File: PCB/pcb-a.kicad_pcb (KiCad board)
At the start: 2 copper layers, 109.7 x 43.5 mm, 44 parts, among them Q1 BC327, Q3 BC337, SW1 config, U1 MCP23008-xP, U2 MAX232I, U4 ATmega16L-8P, Y1 8Mhz

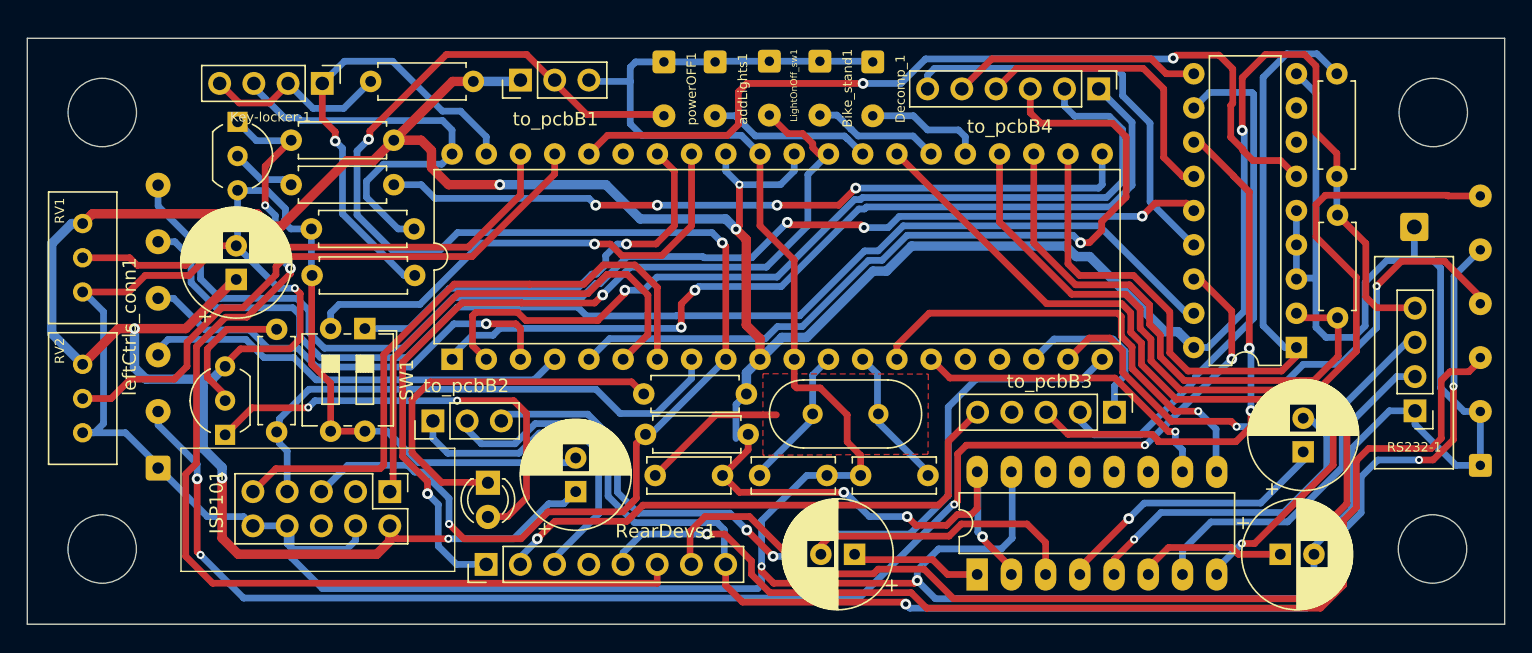
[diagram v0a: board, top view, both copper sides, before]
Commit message: Pin-header connectors adjustment
The main idea to mount the two pcb-A on the pcbB has been dropped, because the result is a too much chatic one and I realized that
wires welder on the top is a dangerous solution, they can create unwanted contacts and short-circuits... So, I choise to place the
two PCB beside. So, in order to get a more ordered and clean solution, I am using flat cables instead wires, and pin-header
connectors instead of welding them directly. I foung good connectors where every female-plug is blocked in its male-socket. But,
they are available just for even numbers of pins. For this reason, I have adjusted all the pin-header connectors and their
positions.
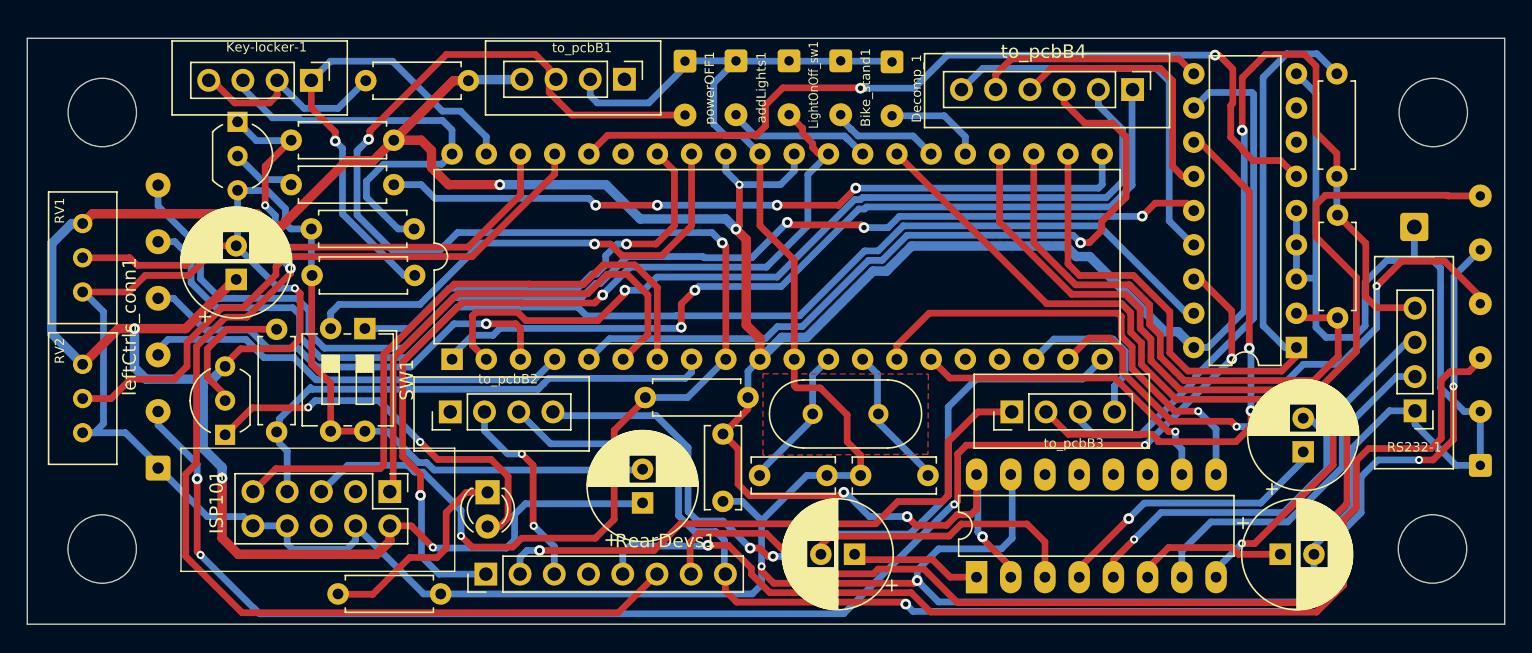
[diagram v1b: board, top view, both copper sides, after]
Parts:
- to_pcbB1, to_pcbB2: value Conn_01x03 -> Conn_01x04; footprint Connector_PinHeader_2.54mm:PinHeader_1x03_P2.54mm_Vertical -> Connector_PinHeader_2.54mm:PinHeader_1x04_P2.54mm_Vertical
- to_pcbB3: value Conn_01x05 -> Conn_01x04; footprint Connector_PinHeader_2.54mm:PinHeader_1x05_P2.54mm_Vertical -> Connector_PinHeader_2.54mm:PinHeader_1x04_P2.54mm_Vertical
- moved R9 27.1 mm to (125.4, 101.9)
- moved to_pcbB1 7.72 mm to (146.7, 63.7), turned to -90 degrees
- moved to_pcbB3 7.62 mm to (175.4, 88.4), turned to 90 degrees
- moved C7 5.03 mm to (148.0, 95.1)
- moved C2 3.08 mm to (154.0, 90.0), turned to -90 degrees
- moved R2 2.74 mm to (155.8, 87.3)
- moved to_pcbB4 2.52 mm to (184.4, 64.5)
- moved powerOFF1 1.56 mm to (151.2, 62.3)
- moved addLights1 1.55 mm to (154.9, 62.3)
- moved Bike_stand1 1.55 mm to (162.7, 62.3)
- moved LightOnOff_sw1 1.46 mm to (158.9, 62.3)
- moved to_pcbB2 1.45 mm to (133.7, 88.4)
- moved Decomp_1 1.43 mm to (166.5, 62.4)
- moved Key-locker-1 0.84 mm to (123.4, 63.8)
- moved RearDevs1 0.72 mm to (136.4, 100.4)
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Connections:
- to_pcbB1 pad 1: tempPower -> unconnected-(to_pcbB1-Pin_1-Pad1)
- to_pcbB1 pad 2: i_powerOFF -> GND
- to_pcbB1 pad 3: GND -> i_powerOFF
- to_pcbB2 pad 1: c_rightArrow -> unconnected-(to_pcbB2-Pin_1-Pad1)
- to_pcbB2 pad 2: c_engineOFF -> c_rightArrow
- to_pcbB2 pad 3: o_engineON -> c_engineOFF
- to_pcbB3 pad 1: o_keepAlive -> c_leftArrow
- to_pcbB3 pad 2: o_engineReady -> o_neutral
- to_pcbB3 pad 3: o_neutral -> o_engineReady
- to_pcbB3 pad 4: unconnected-(to_pcbB3-Pin_4-Pad4) -> o_keepAlive
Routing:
- net Net-(D1-K): track 28.5 -> 15.8 mm
- net c_rightArrow: track 25.0 -> 14.9 mm, vias 0 -> 2
- net GND: track 381.0 -> 372.8 mm
- net tempPower: track 302.1 -> 306.9 mm
- net i_powerOFF: track 112.6 -> 117.4 mm
- net c_engineOFF: track 108.5 -> 104.0 mm
- net Net-(D1-A): track 33.6 -> 29.3 mm
- net o_engineON: track 61.6 -> 57.9 mm
- net c_leftArrow: track 41.3 -> 44.6 mm
- net o_addLight: track 59.8 -> 56.8 mm
- net o_upLight: track 66.8 -> 64.3 mm
- net o_rightArrow: track 18.6 -> 16.8 mm
- net o_horn: track 21.6 -> 19.9 mm
- net Net-(ISP101-Pin_7): track 40.4 -> 38.7 mm
- net i_addLight: track 12.1 -> 10.7 mm
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
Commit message: Important fixes and adjustments
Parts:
- moved Q3 3.21 mm to (119.7, 69.5), turned to 180 degrees
- moved C1 0.18 mm to (117.8, 78.4)
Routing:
- net GND: track 372.8 -> 377.6 mm, vias 3 -> 2
- net c_startEngine: track 79.1 -> 75.3 mm
- net Net-(Q3-B): track 4.86 -> 5.57 mm
- net tempPower: track 306.9 -> 306.2 mm

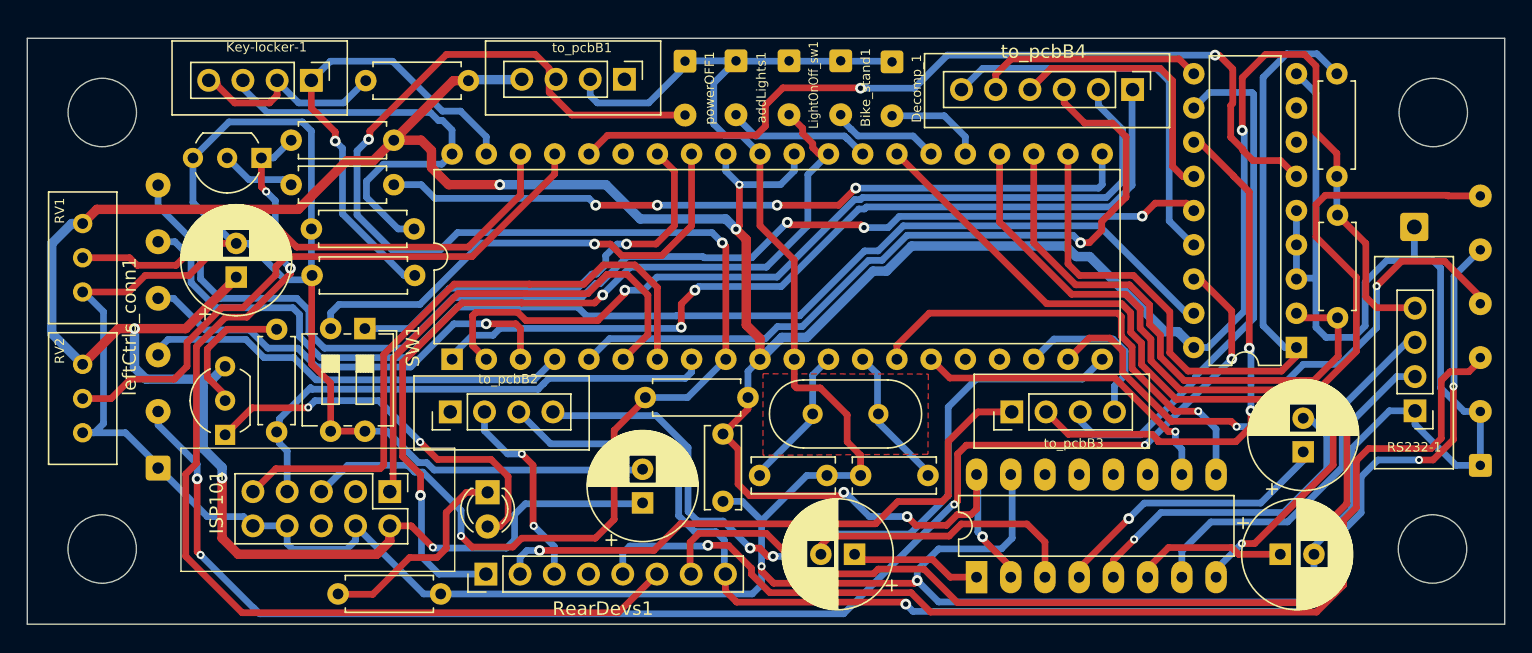
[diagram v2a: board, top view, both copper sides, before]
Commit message: Components positions adjustment
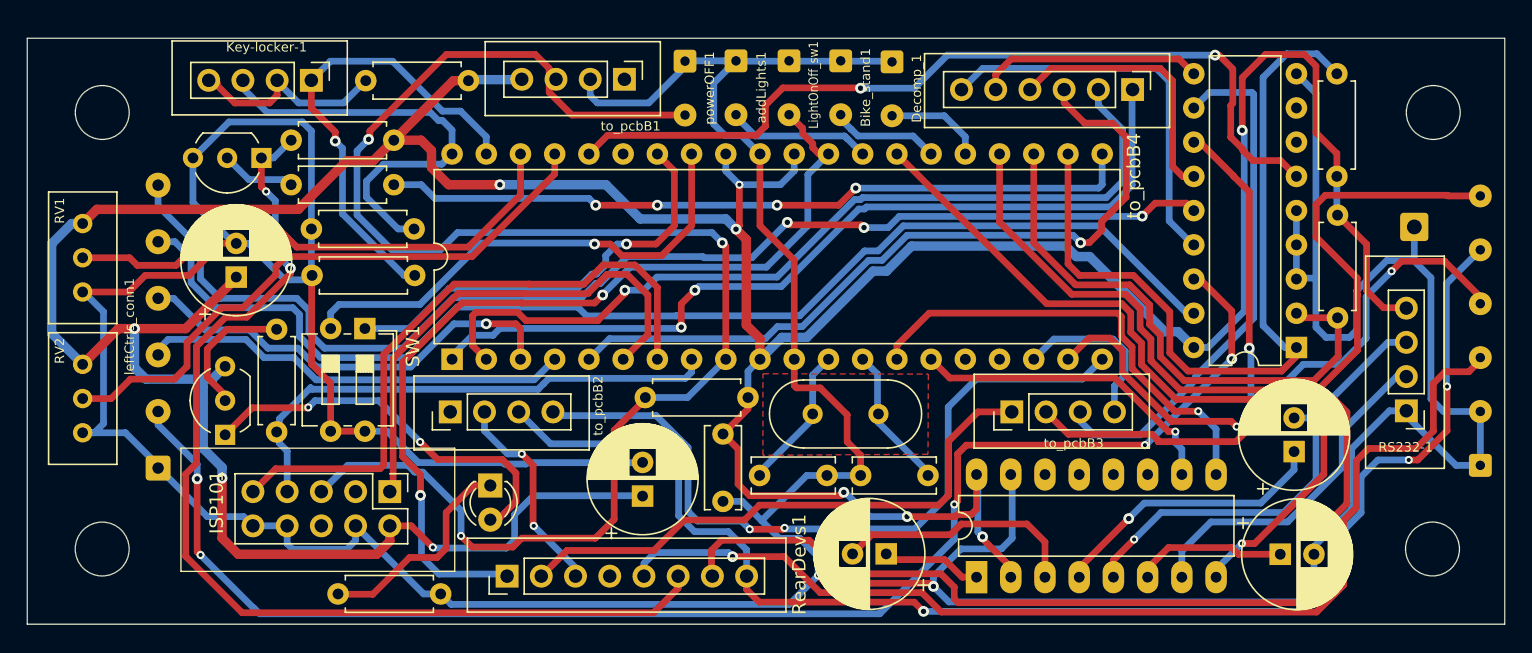
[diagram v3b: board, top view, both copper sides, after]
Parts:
- moved C5 2.35 mm to (166.1, 98.9)
- moved RearDevs1 1.58 mm to (138.0, 100.6)
- moved C6 0.67 mm to (196.4, 91.3)
- moved RS232-1 0.64 mm to (204.7, 88.3)
- moved D1 0.55 mm to (136.7, 93.8)
- moved C7 0.51 mm to (148.0, 94.6)
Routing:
- net c_brakeSwitch: track 82.7 -> 79.7 mm
- net Net-(U2-C1-): track 21.1 -> 18.4 mm
- net Net-(U2-C1+): track 9.76 -> 7.42 mm
- net c_leftArrow: track 44.6 -> 42.3 mm, vias 1 -> 0
- net c_startEngine: track 75.3 -> 77.3 mm
- net i_neutral: track 109.6 -> 107.6 mm
- net c_rearLight: track 65.1 -> 66.8 mm
- net o_engineON: track 57.9 -> 56.3 mm
- net i_leftArrow: track 107.6 -> 109.1 mm
- net tempPower: track 306.2 -> 305.0 mm
- net c_engineOFF: track 104.0 -> 103.0 mm
- net c_rightArrow: track 14.9 -> 15.7 mm
- net Net-(RS232-1-Pin_2): track 26.2 -> 25.5 mm
- net GND: track 377.6 -> 378.1 mm
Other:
- outline, holes or cut-outs redrawn

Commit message: Bike-stand switch has moved in the rear-connector
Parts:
- removed Bike_stand1: Conn_01x02, Connector_Wire:SolderWire-0.15sqmm_1x02_P4mm_D0.5mm_OD1.5mm
- moved LightOnOff_sw1 2.90 mm to (161.8, 62.3)
- moved addLights1 2.59 mm to (157.5, 62.3)
- moved powerOFF1 1.85 mm to (153.0, 62.3)
- moved to_pcbB1 0.74 mm to (147.4, 63.7)
- moved Decomp_1 0.58 mm to (165.9, 62.4)
- moved R1 0.41 mm to (135.5, 63.8)
- moved Key-locker-1 0.38 mm to (123.8, 63.8)
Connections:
- RearDevs1 pad 4: unconnected-(RearDevs1-Pin_4-Pad4) -> i_bykeStand
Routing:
- net i_bykeStand: track 8.10 -> 74.5 mm, vias 0 -> 3
- net i_neutral: track 107.6 -> 110.9 mm
- net i_addLight: track 10.7 -> 8.03 mm
- net i_powerOFF: track 117.4 -> 119.8 mm
- net GND: track 378.1 -> 375.9 mm
- net Net-(ISP101-Pin_9): track 47.8 -> 49.6 mm
- net Net-(ISP101-Pin_1): track 37.7 -> 39.3 mm
- net o_addLight: track 56.8 -> 58.2 mm
- net i_rightArrow: track 89.8 -> 88.5 mm
- net tempPower: track 305.0 -> 305.6 mm
- net i_decompr: track 7.36 -> 7.95 mm
- net i_Vx2: track 35.3 -> 34.8 mm

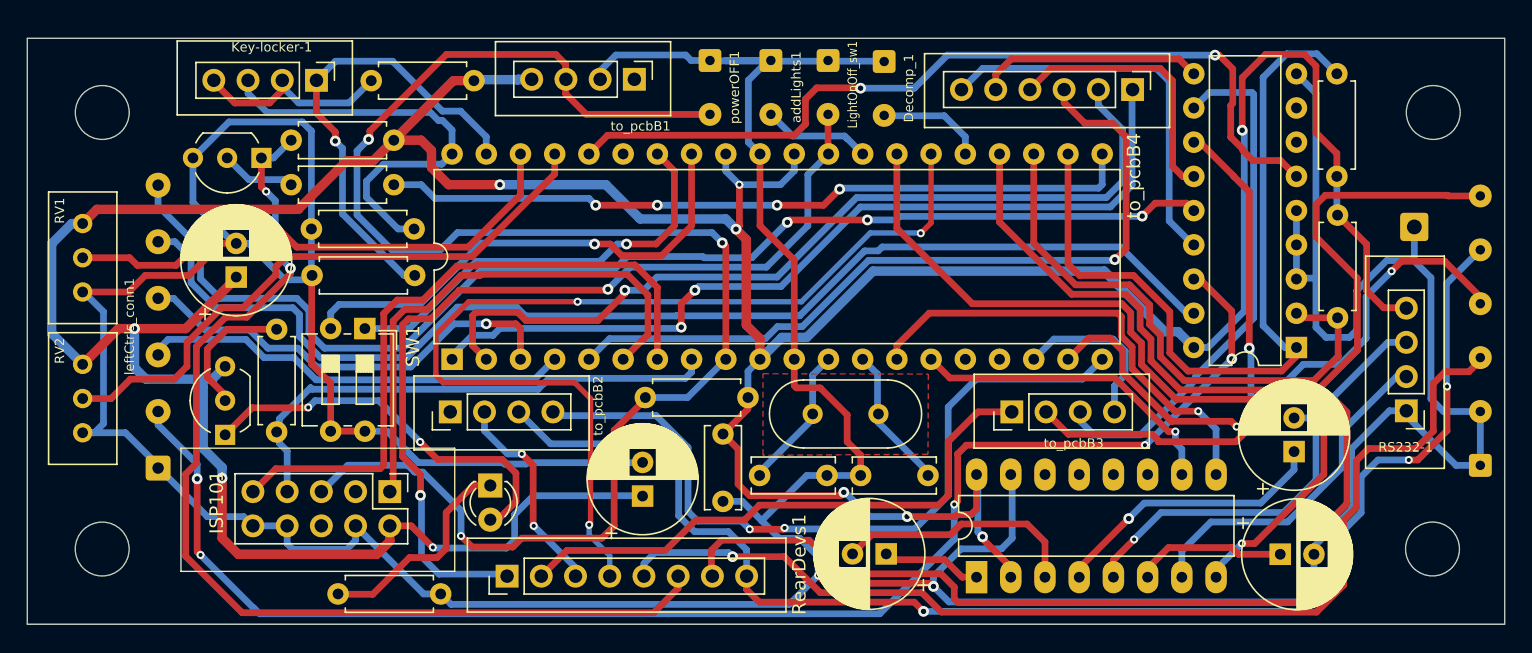
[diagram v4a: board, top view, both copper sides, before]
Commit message: 20 Ohm resistor added for MAX232
I got overheating experience on that chip. So, I looked for some info on internet. But I found just a post that suggest to add
the resistor to prevent capacitor dircharge trouble. I have tried the solution and it looks like function very well. But don't
ask me why!!! :-(
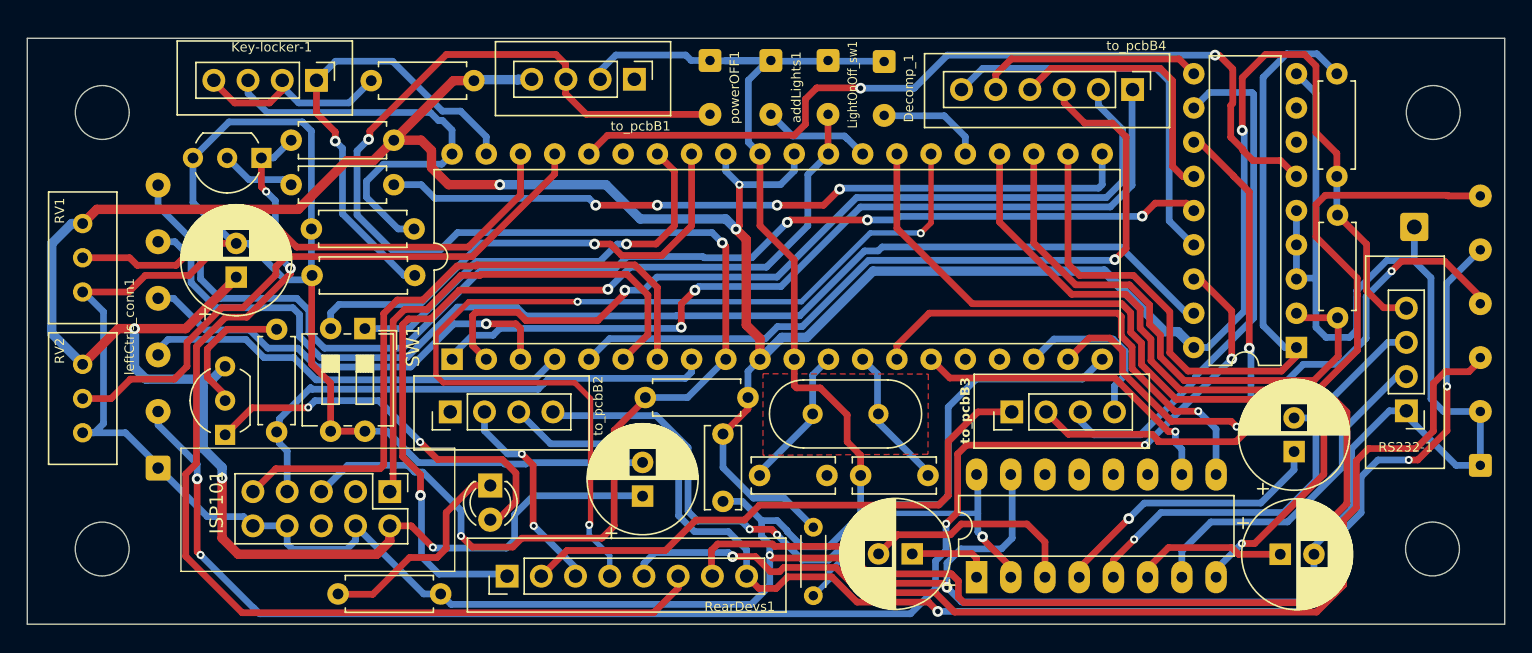
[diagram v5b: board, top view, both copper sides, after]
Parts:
- added R11: 20, Resistor_THT:R_Axial_DIN0204_L3.6mm_D1.6mm_P5.08mm_Horizontal, F.Cu at (160.7, 96.9)
- moved C5 1.93 mm to (168.0, 98.9)
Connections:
- U2 pad 16: tempPower -> Net-(U2-VCC)
- U2 pad 2: tempPower -> Net-(U2-VCC)
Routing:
- net Net-(U2-VCC): track 0.00 -> 23.8 mm, vias 0 -> 1
- net tempPower: track 305.6 -> 282.1 mm, vias 10 -> 7
- net Net-(U2-C1-): track 18.4 -> 16.4 mm
- net o_engineON: track 56.3 -> 58.2 mm
- net GND: track 375.9 -> 377.6 mm
- net i_leftArrow: track 109.1 -> 110.4 mm
- net Net-(U2-C1+): track 7.42 -> 6.33 mm

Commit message: Parking button added and Horn management removed
Horn is connected directly to the power PCB
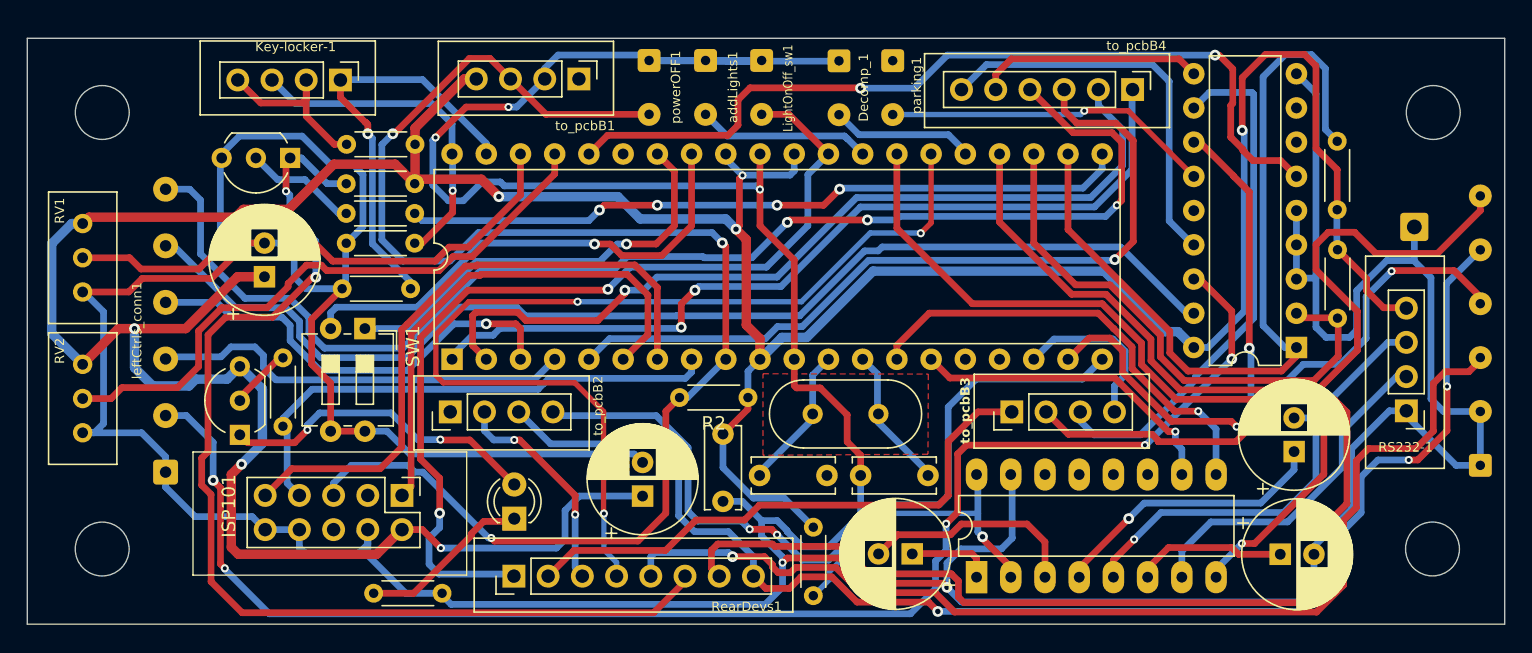
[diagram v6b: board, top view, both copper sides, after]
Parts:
- added parking1: Conn_01x02, Connector_Wire:SolderWire-0.15sqmm_1x02_P4mm_D0.5mm_OD1.5mm, F.Cu at (166.6, 62.3)
- R1, R10, R2, R3, R4, R5, R6, R7, R8, R9: footprint Resistor_THT:R_Axial_DIN0207_L6.3mm_D2.5mm_P7.62mm_Horizontal -> Resistor_THT:R_Axial_DIN0204_L3.6mm_D1.6mm_P5.08mm_Horizontal
- moved R1 6.43 mm to (131.1, 68.5)
- moved R6 5.21 mm to (126.0, 71.4)
- moved LightOnOff_sw1 4.93 mm to (156.9, 62.3)
- moved addLights1 4.85 mm to (152.7, 62.3)
- moved R7 4.61 mm to (126.0, 73.6)
- moved powerOFF1 4.52 mm to (148.5, 62.3)
- moved to_pcbB1 4.11 mm to (143.3, 63.7)
- moved Decomp_1 3.35 mm to (162.6, 62.3)
- moved D1 3.04 mm to (138.5, 96.3), turned to 90 degrees
- moved R9 2.64 mm to (128.0, 101.8)
- moved R5 2.57 mm to (199.6, 76.3)
- moved R10 2.47 mm to (199.6, 73.4)
- moved R8 2.17 mm to (121.3, 84.4)
- moved Q3 2.13 mm to (121.9, 69.5)
- moved C1 2.10 mm to (119.9, 78.3)
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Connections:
- U1 pad 13: o_horn -> i_parking
- U1 pad 14: i_horn -> unconnected-(U1-GP4-Pad14)
- leftCtrls_conn1 pad 6: i_horn -> c_horn
- to_pcbB4 pad 4: o_horn -> c_horn
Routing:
- net c_horn: track 0.00 -> 96.2 mm, vias 0 -> 3
- net i_horn: track 89.8 -> 0.00 mm, vias 3 -> 0
- net GND: track 377.6 -> 432.4 mm, vias 2 -> 5
- net i_parking: track 0.00 -> 24.5 mm, vias 0 -> 1
- net o_horn: track 19.9 -> 0.00 mm
- net i_powerOFF: track 119.8 -> 110.1 mm
- net i_Vx1: track 31.9 -> 25.1 mm, vias 0 -> 1
- net Net-(D1-A): track 29.4 -> 23.9 mm
- net Net-(Q1-B): track 9.90 -> 4.65 mm
- net i_addLight: track 8.03 -> 12.9 mm
- net c_startEngine: track 77.3 -> 80.9 mm
- net i_Vx2: track 34.8 -> 31.2 mm
- net Net-(D1-K): track 16.2 -> 12.8 mm
- net Net-(Q3-B): track 5.57 -> 8.41 mm
- net i_decompr: track 7.95 -> 10.7 mm
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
